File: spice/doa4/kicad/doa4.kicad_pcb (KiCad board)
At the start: 2 copper layers, 28 parts, among them Q1 BC557, Q10 BC547, Q11 BD139, Q12 BD140, Q2 BC557, Q3 BC547, Q4 BC547, Q5 BC557, Q6 BC547, Q7 BC547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

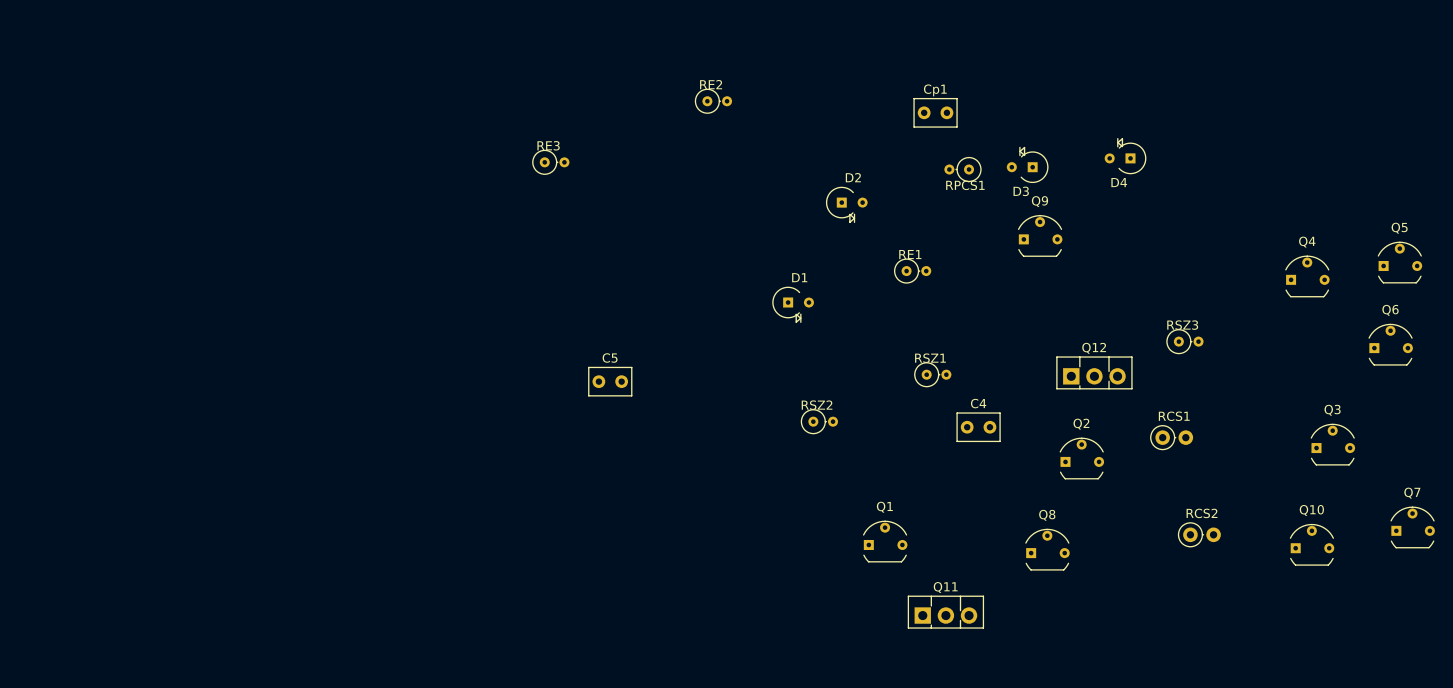
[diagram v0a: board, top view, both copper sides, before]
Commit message: init location input
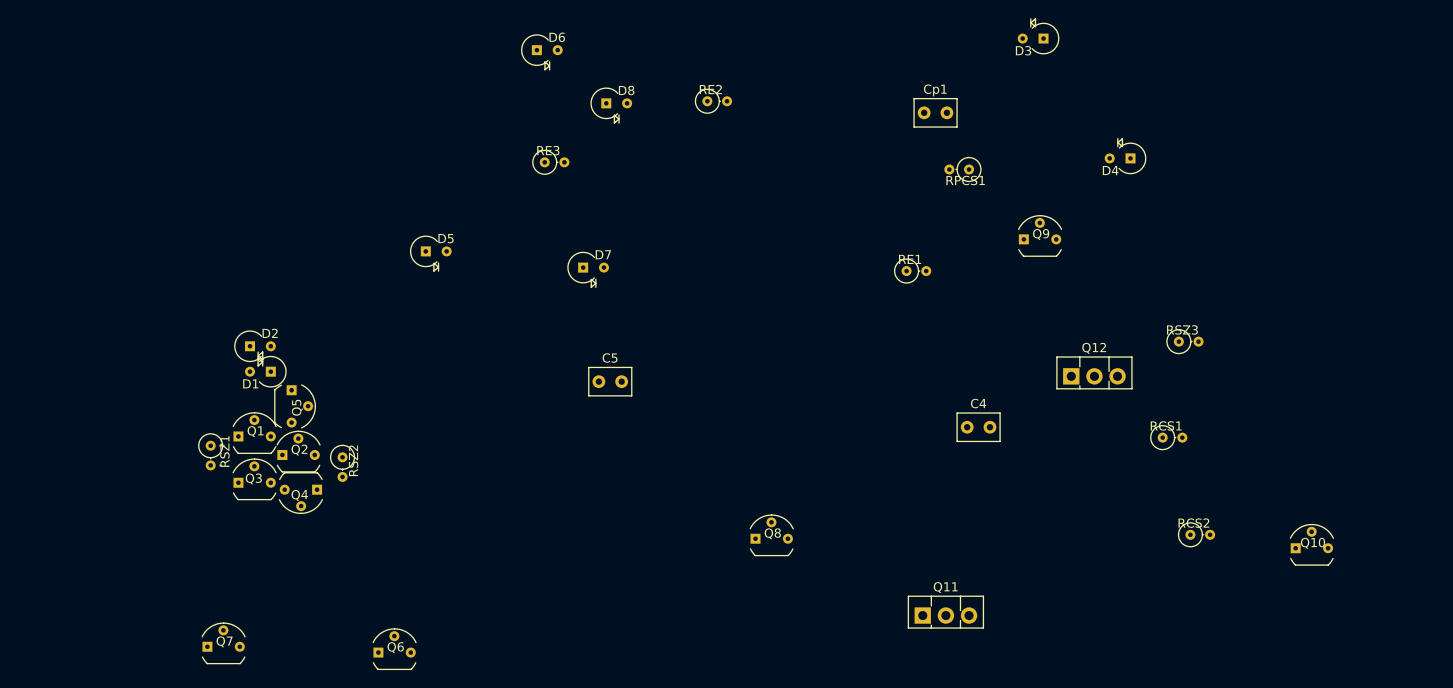
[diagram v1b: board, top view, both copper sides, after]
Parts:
- added D5: D1N4148, Doa4FPLibrary:D_DO-41_SOD81_P2.54mm_Vertical_AnodeUp_Doa4, F.Cu at (82.8, 71.9)
- added D6: D1N4148, Doa4FPLibrary:D_DO-41_SOD81_P2.54mm_Vertical_AnodeUp_Doa4, F.Cu at (95.0, 49.8)
- added D7: D1N4148, Doa4FPLibrary:D_DO-41_SOD81_P2.54mm_Vertical_AnodeUp_Doa4, F.Cu at (100.1, 73.7)
- added D8: D1N4148, Doa4FPLibrary:D_DO-41_SOD81_P2.54mm_Vertical_AnodeUp_Doa4, F.Cu at (102.6, 55.6)
- D3: value D14148 -> D1N4148
- D4: value D1418 -> D1N4148
- RCS1, RCS2: footprint Resistors_THT:R_Axial_DIN0207_L6.3mm_D2.5mm_P2.54mm_Vertical -> Doa4FPLibrary:R_Axial_DIN0207_L6.3mm_D2.5mm_P2.54mm_Vertical_Doa4
- moved Q7 131.1 mm to (58.1, 115.3)
- moved Q5 119.8 mm to (68.1, 86.4), turned to 270 degrees
- moved Q3 118.4 mm to (61.5, 97.3)
- moved Q6 114.3 mm to (76.8, 115.9)
- moved Q4 107.9 mm to (71.6, 98.0), turned to 180 degrees
- moved Q2 86.0 mm to (66.3, 94.2)
- moved RSZ1 79.0 mm to (59.2, 93.2), turned to 270 degrees
- moved Q1 70.2 mm to (61.5, 92.2)
- moved D2 66.9 mm to (63.5, 82.3)
- moved D1 57.3 mm to (65.8, 85.1), turned to 180 degrees
- moved RSZ2 51.8 mm to (73.7, 94.5), turned to 270 degrees
- moved Q8 30.3 mm to (118.2, 103.4)
- moved D3 14.2 mm to (150.6, 48.5)
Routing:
- net (no net): track 0.00 -> 0.58 mm

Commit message: conn j990 added
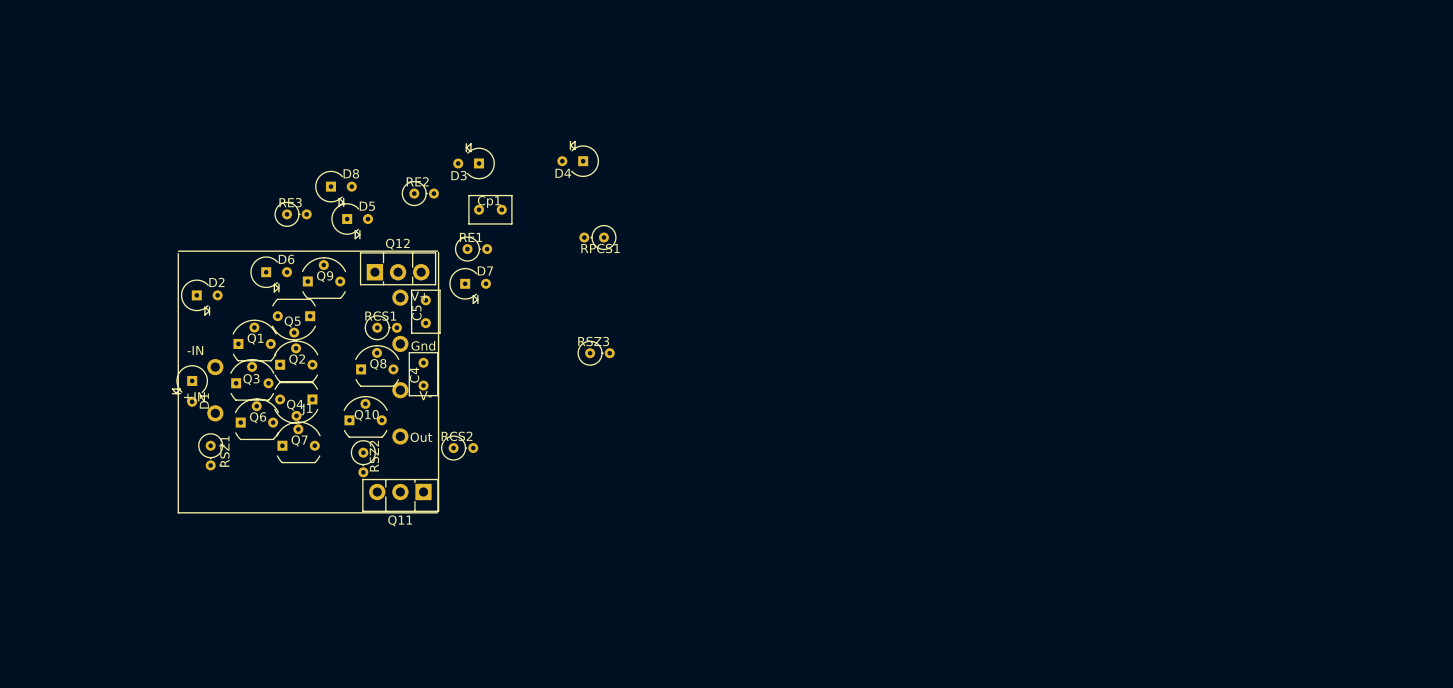
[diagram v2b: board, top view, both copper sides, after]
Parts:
- added J1: CONN_01X06, Doa4FPLibrary:j990, F.Cu at (69.8, 87.1)
- C4: footprint Capacitors_THT:C_Rect_L4.6mm_W3.0mm_P2.50mm_MKS02_FKP02 -> Doa4FPLibrary:C_Rect_L4.6mm_W3.0mm_P2.50mm_MKS02_FKP02_Doa4
- moved Q10 104.8 mm to (73.7, 90.4)
- moved RCS1 87.1 mm to (77.5, 80.3)
- moved RCS2 81.5 mm to (85.9, 93.5)
- moved Q9 78.7 mm to (69.1, 75.2)
- moved Q12 77.3 mm to (77.2, 74.2)
- moved RSZ3 64.7 mm to (100.8, 83.1)
- moved D3 63.5 mm to (88.6, 62.2)
- moved D4 60.1 mm to (100.1, 62.0)
- moved C4 59.9 mm to (82.5, 86.6), turned to 90 degrees
- moved Q11 56.5 mm to (82.5, 98.3), turned to 180 degrees
- moved Cp1 50.0 mm to (88.6, 67.3)
- moved RE1 48.3 mm to (87.4, 71.6)
- moved Q8 47.1 mm to (74.9, 84.8)
- moved RPCS1 40.8 mm to (102.4, 70.4)
- moved D6 38.4 mm to (65.3, 74.2)
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
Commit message: location init
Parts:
- added RCP1: 380, Doa4FPLibrary:R_Axial_DIN0207_L6.3mm_D2.5mm_P2.54mm_Vertical_Doa4, F.Cu at (64.0, 72.9)
- moved D4 43.3 mm to (58.4, 73.7), turned to 0 degrees
- moved D3 32.6 mm to (58.9, 75.7), turned to 270 degrees
- moved Q6 32.1 mm to (93.7, 93.2), turned to 270 degrees
- moved RSZ3 31.3 mm to (73.7, 98.6), turned to 180 degrees
- moved RE3 28.8 mm to (77.0, 95.0)
- moved RPCS1 28.6 mm to (73.9, 73.4)
- moved Cp1 28.0 mm to (62.0, 75.9)
- moved Q12 24.9 mm to (77.5, 99.1)
- moved Q11 24.9 mm to (82.5, 73.4)
- moved RCS1 21.3 mm to (56.6, 75.9), turned to 270 degrees
- moved D6 20.9 mm to (71.1, 94.2)
- moved RE1 17.0 mm to (70.9, 75.7)
- moved RCS2 16.7 mm to (88.4, 77.0), turned to 270 degrees
- moved Q9 15.3 mm to (74.7, 89.4)
- moved Q5 15.2 mm to (55.9, 81.3), turned to 0 degrees
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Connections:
- Cp1 pad 1: /ODiff -> Net-(Cp1-Pad1)
- Q10 pad 1: Net-(Cp1-Pad2) -> Net-(Q10-Pad1)
- Q9 pad 2: Net-(Cp1-Pad2) -> Net-(Q10-Pad1)
- RSZ3 pad 1: Net-(Cp1-Pad2) -> Net-(Q10-Pad1)
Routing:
- net /In-: track 0.00 -> 6.48 mm
- net /In+: track 0.00 -> 5.85 mm
- net (no net): track 0.58 -> 0.00 mm

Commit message: location init 2
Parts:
- moved Q6 31.1 mm to (63.1, 87.9)
- moved D4 29.2 mm to (73.4, 98.7), turned to 180 degrees
- moved Q8 25.1 mm to (65.4, 76.6)
- moved RCS1 23.8 mm to (72.9, 93.3)
- moved Q4 23.2 mm to (55.8, 76.6), turned to 0 degrees
- moved RCS2 23.2 mm to (65.5, 73.0), turned to 180 degrees
- moved Q5 21.4 mm to (69.5, 97.8), turned to 180 degrees
- moved D3 20.2 mm to (67.2, 94.1), turned to 0 degrees
- moved RSZ3 18.1 mm to (66.2, 82.0), turned to 0 degrees
- moved RSZ2 17.8 mm to (62.4, 76.6)
- moved RCP1 16.3 mm to (72.4, 86.9), turned to 180 degrees
- moved RE1 14.8 mm to (74.3, 90.0)
- moved Q2 13.1 mm to (60.8, 80.4), turned to 180 degrees
- moved Cp1 12.0 mm to (71.5, 83.3)
- moved Q10 7.59 mm to (66.3, 88.5)
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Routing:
- net /In-: track 6.48 -> 0.00 mm
- net /In+: track 5.85 -> 0.00 mm

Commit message: location init 3 power
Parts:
- moved D3 2.57 mm to (69.7, 94.5), turned to 180 degrees
- moved Q7 1.26 mm to (63.9, 84.1)
- moved RSZ3 1.15 mm to (67.3, 82.2)
- moved RSZ2 1.02 mm to (62.9, 75.7)
- moved Q4 0.92 mm to (56.5, 76.1)
- moved Q2 0.91 mm to (61.6, 79.9)
- moved Q5 0.74 mm to (69.1, 97.2)
- moved Q11 0.72 mm to (82.0, 73.9)
- moved Q9 0.63 mm to (69.1, 92.8)
- moved RCP1 0.63 mm to (72.9, 86.5)
- moved Q6 0.61 mm to (63.7, 87.9)
- moved Q12 0.54 mm to (77.1, 98.7)
- moved RCS2 0.54 mm to (65.2, 73.4)
- moved RE3 0.54 mm to (80.8, 94.9)
- moved Q3 0.28 mm to (61.5, 97.4)
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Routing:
- net /V-: track 0.00 -> 30.6 mm
- net /V+: track 0.00 -> 19.9 mm
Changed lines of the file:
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@@
   (general
     (links 60)
-    (no_connects 60)
+    (no_connects 54)
     (area 52.478438 69.161 84.8315 103.405)
     (thickness 1.6)
     (drawings 0)
-    (tracks 0)
+    (tracks 17)
     (zones 0)
     (modules 34)
@@
     (44 Edge.Cuts user hide)
     (45 Margin user)
-    (46 B.CrtYd user)
+    (46 B.CrtYd user hide)
     (47 F.CrtYd user hide)
     (48 B.Fab user hide)
@@
   )
   (module Doa4FPLibrary:TO-126_Vertical_Doa4 (layer F.Cu)
-    (at 82.55 73.406 180)
+    (at 82.042 73.914 180)
     (descr "TO-126, Vertical, RM 2.54mm")
     (tags "TO-126 Vertical RM 2.54mm")
@@
   )
   (module Doa4FPLibrary:TO-126_Vertical_Doa4 (layer F.Cu)
-    (at 77.47 99.06)
+    (at 77.089 98.679)
     (descr "TO-126, Vertical, RM 2.54mm")
     (tags "TO-126 Vertical RM 2.54mm")
@@
   )
   (module Doa4FPLibrary:TO-92_Molded_Wide_BCXXX (layer F.Cu)
-    (at 66.294 88.519 90)
+    (at 66.548 88.646 90)
     (descr "TO-92 leads molded, wide, drill 0.8mm (see NXP sot054_po.pdf)")
     (tags "to-92 sc-43 sc-43a sot54 PA33 transistor")
@@
   )
   (module Doa4FPLibrary:TO-92_Molded_Wide_BCXXX (layer F.Cu)
-    (at 68.58 93.218 90)
+    (at 69.088 92.837 90)
     (descr "TO-92 leads molded, wide, drill 0.8mm (see NXP sot054_po.pdf)")
     (tags "to-92 sc-43 sc-43a sot54 PA33 transistor")
@@
   )
   (module Doa4FPLibrary:TO-92_Molded_Wide_BCXXX (layer F.Cu)
-    (at 62.992 84.963 90)
+    (at 63.881 84.074 90)
     (descr "TO-92 leads molded, wide, drill 0.8mm (see NXP sot054_po.pdf)")
     (tags "to-92 sc-43 sc-43a sot54 PA33 transistor")
@@
   )
   (module Doa4FPLibrary:TO-92_Molded_Wide_BCXXX (layer F.Cu)
-    (at 63.119 87.884 270)
+    (at 63.7286 87.9094 270)
     (descr "TO-92 leads molded, wide, drill 0.8mm (see NXP sot054_po.pdf)")
     (tags "to-92 sc-43 sc-43a sot54 PA33 transistor")
@@
   )
   (module Doa4FPLibrary:TO-92_Molded_Wide_BCXXX (layer F.Cu)
-    (at 69.469 97.79 180)
+    (at 69.088 97.155 180)
     (descr "TO-92 leads molded, wide, drill 0.8mm (see NXP sot054_po.pdf)")
     (tags "to-92 sc-43 sc-43a sot54 PA33 transistor")
@@
   )
   (module Doa4FPLibrary:TO-92_Molded_Wide_BCXXX (layer F.Cu)
-    (at 55.753 76.581)
+    (at 56.515 76.073)
     (descr "TO-92 leads molded, wide, drill 0.8mm (see NXP sot054_po.pdf)")
     (tags "to-92 sc-43 sc-43a sot54 PA33 transistor")
@@
   )
   (module Doa4FPLibrary:TO-92_Molded_Wide_BCXXX (layer F.Cu)
-    (at 61.214 97.282 180)
+    (at 61.468 97.409 180)
     (descr "TO-92 leads molded, wide, drill 0.8mm (see NXP sot054_po.pdf)")
     (tags "to-92 sc-43 sc-43a sot54 PA33 transistor")
@@
   )
   (module Doa4FPLibrary:TO-92_Molded_Wide_BCXXX (layer F.Cu)
-    (at 60.833 80.391 180)
+    (at 61.5696 79.8576 180)
     (descr "TO-92 leads molded, wide, drill 0.8mm (see NXP sot054_po.pdf)")
     (tags "to-92 sc-43 sc-43a sot54 PA33 transistor")
@@
   )
   (module Doa4FPLibrary:TO-92_Molded_Wide_BCXXX (layer F.Cu)
-    (at 56.134 93.472)
+    (at 56.388 93.472)
     (descr "TO-92 leads molded, wide, drill 0.8mm (see NXP sot054_po.pdf)")
     (tags "to-92 sc-43 sc-43a sot54 PA33 transistor")
@@
   )
   (module Doa4FPLibrary:R_Axial_DIN0207_L6.3mm_D2.5mm_P2.54mm_Vertical_Doa4 (layer F.Cu)
-    (at 62.357 76.581 270)
+    (at 62.865 75.692 270)
     (descr "Resistor, Axial_DIN0207 series, Axial, Vertical, pin pitch=2.54mm, 0.25W = 1/4W, length*diameter=6.3*2.5mm^2, http://cdn-reichelt.de/documents/datenblatt/B400/1_4W%23YAG.pdf")
     (tags "Resistor Axial_DIN0207 series Axial Vertical pin pitch 2.54mm 0.25W = 1/4W length 6.3mm diameter 2.5mm")
@@
   )
   (module Doa4FPLibrary:R_Axial_DIN0207_L6.3mm_D2.5mm_P2.54mm_Vertical_Doa4 (layer F.Cu)
-    (at 65.532 73.025 180)
+    (at 65.151 73.406 180)
     (descr "Resistor, Axial_DIN0207 series, Axial, Vertical, pin pitch=2.54mm, 0.25W = 1/4W, length*diameter=6.3*2.5mm^2, http://cdn-reichelt.de/documents/datenblatt/B400/1_4W%23YAG.pdf")
     (tags "Resistor Axial_DIN0207 series Axial Vertical pin pitch 2.54mm 0.25W = 1/4W length 6.3mm diameter 2.5mm")
@@
   )
   (module Doa4FPLibrary:R_Axial_DIN0207_L6.3mm_D2.5mm_P2.54mm_Vertical_Doa4 (layer F.Cu)
-    (at 66.167 82.042)
+    (at 67.31 82.169)
     (descr "Resistor, Axial_DIN0207 series, Axial, Vertical, pin pitch=2.54mm, 0.25W = 1/4W, length*diameter=6.3*2.5mm^2, http://cdn-reichelt.de/documents/datenblatt/B400/1_4W%23YAG.pdf")
     (tags "Resistor Axial_DIN0207 series Axial Vertical pin pitch 2.54mm 0.25W = 1/4W length 6.3mm diameter 2.5mm")
@@
   )
   (module Doa4FPLibrary:R_Axial_DIN0207_L6.3mm_D2.5mm_P2.54mm_Vertical_Doa4 (layer F.Cu)
-    (at 81.153 95.25)
+    (at 80.772 94.869)
     (descr "Resistor, Axial_DIN0207 series, Axial, Vertical, pin pitch=2.54mm, 0.25W = 1/4W, length*diameter=6.3*2.5mm^2, http://cdn-reichelt.de/documents/datenblatt/B400/1_4W%23YAG.pdf")
     (tags "Resistor Axial_DIN0207 series Axial Vertical pin pitch 2.54mm 0.25W = 1/4W length 6.3mm diameter 2.5mm")
@@
   )
   (module Doa4FPLibrary:D_DO-41_SOD81_P2.54mm_Vertical_AnodeUp_Doa4 (layer F.Cu)
-    (at 67.183 94.107)
+    (at 69.723 94.488 180)
     (descr "D, DO-41_SOD81 series, Axial, Vertical, pin pitch=2.54mm, , length*diameter=5.2*2.7mm^2, , http://www.diodes.com/_files/packages/DO-41%20(Plastic).pdf")
     (tags "D DO-41_SOD81 series Axial Vertical pin pitch 2.54mm  length 5.2mm diameter 2.7mm")
-    (fp_text reference D3 (at 2.2098 -1.3716) (layer F.SilkS)
-      (effects (font (size 1 1) (thickness 0.15)))
-    )
-    (fp_text value D1N4148 (at 0.9398 1.0668) (layer F.Fab)
+    (fp_text reference D3 (at 2.2098 -1.3716 180) (layer F.SilkS)
+      (effects (font (size 1 1) (thickness 0.15)))
+    )
+    (fp_text value D1N4148 (at 0.9398 1.0668 180) (layer F.Fab)
       (effects (font (size 1 1) (thickness 0.15)))
     )
@@
     (fp_line (start 0 0) (end 2.54 0) (layer F.Fab) (width 0.1))
     (fp_line (start 1.397 1.28) (end 1.397 2.169) (layer F.SilkS) (width 0.12))
-    (fp_text user K (at 3.2512 0) (layer F.Fab)
-      (effects (font (size 1 1) (thickness 0.15)))
-    )
-    (pad 1 thru_hole rect (at 0 0) (size 1.1 1.1) (drill 0.5) (layers *.Cu *.Mask)
+    (fp_text user K (at 3.2512 0 180) (layer F.Fab)
+      (effects (font (size 1 1) (thickness 0.15)))
+    )
+    (pad 1 thru_hole rect (at 0 0 180) (size 1.1 1.1) (drill 0.5) (layers *.Cu *.Mask)
       (net 21 "Net-(D3-Pad1)"))
-    (pad 2 thru_hole oval (at 2.286 0) (size 1.1 1.1) (drill 0.5) (layers *.Cu *.Mask)
+    (pad 2 thru_hole oval (at 2.286 0 180) (size 1.1 1.1) (drill 0.5) (layers *.Cu *.Mask)
       (net 9 /VrefCS))
     (model Diodes_THT.3dshapes/D_DO-41_SOD81_P2.54mm_Vertical_AnodeUp.wrl
@@
   )
   (module Doa4FPLibrary:C_Rect_L4.6mm_W3.0mm_P2.50mm_MKS02_FKP02_Doa4 (layer F.Cu)
-    (at 82.804 83.82 270)
+    (at 82.55 83.86 270)
     (descr "C, Rect series, Radial, pin pitch=2.50mm, , length*width=4.6*3.0mm^2, Capacitor, http://www.wima.de/DE/WIMA_MKS_02.pdf")
     (tags "C Rect series Radial pin pitch 2.50mm  length 4.6mm width 3.0mm Capacitor")
@@
   )
   (module Doa4FPLibrary:C_Rect_L4.6mm_W3.0mm_P2.50mm_MKS02_FKP02_Doa4 (layer F.Cu)
-    (at 82.804 78.486 270)
+    (at 82.55 78.486 270)
     (descr "C, Rect series, Radial, pin pitch=2.50mm, , length*width=4.6*3.0mm^2, Capacitor, http://www.wima.de/DE/WIMA_MKS_02.pdf")
     (tags "C Rect series Radial pin pitch 2.50mm  length 4.6mm width 3.0mm Capacitor")
@@
   )
   (module Doa4FPLibrary:R_Axial_DIN0207_L6.3mm_D2.5mm_P2.54mm_Vertical_Doa4 (layer F.Cu)
-    (at 72.39 86.868 180)
+    (at 72.898 86.487 180)
     (descr "Resistor, Axial_DIN0207 series, Axial, Vertical, pin pitch=2.54mm, 0.25W = 1/4W, length*diameter=6.3*2.5mm^2, http://cdn-reichelt.de/documents/datenblatt/B400/1_4W%23YAG.pdf")
     (tags "Resistor Axial_DIN0207 series Axial Vertical pin pitch 2.54mm 0.25W = 1/4W length 6.3mm diameter 2.5mm")
@@
     )
   )
+  (segment (start 73.318001 96.379001) (end 73.773001 95.924001) (width 0.25) (layer B.Cu) (net 1))
+  (segment (start 72.124997 96.379001) (end 73.318001 96.379001) (width 0.25) (layer B.Cu) (net 1))
+  (segment (start 73.773001 94.220001) (end 73.447999 93.894999) (width 0.25) (layer B.Cu) (net 1))
+  (segment (start 73.447999 93.894999) (end 72.898 93.345) (width 0.25) (layer B.Cu) (net 1))
+  (segment (start 73.773001 95.924001) (end 73.773001 94.220001) (width 0.25) (layer B.Cu) (net 1))
+  (segment (start 73.406 98.679) (end 73.406 96.52) (width 0.25) (layer B.Cu) (net 1))
+  (segment (start 79.121001 76.073001) (end 70.510003 76.073001) (width 0.25) (layer B.Cu) (net 1))
+  (segment (start 70.510003 76.073001) (end 67.462002 73.025) (width 0.25) (layer B.Cu) (net 1))
+  (segment (start 83.775001 74.422) (end 83.775001 72.245999) (width 0.25) (layer B.Cu) (net 11))
+  (segment (start 83.775001 74.566001) (end 83.775001 74.422) (width 0.25) (layer B.Cu) (net 11))
+  (segment (start 83.775001 74.422) (end 83.775001 85.348999) (width 0.25) (layer B.Cu) (net 11))
+  (segment (start 83.710001 72.180999) (end 72.980001 72.180999) (width 0.25) (layer B.Cu) (net 11))
+  (segment (start 83.775001 72.245999) (end 83.710001 72.180999) (width 0.25) (layer B.Cu) (net 11))
+  (segment (start 72.980001 72.180999) (end 72.304999 72.856001) (width 0.25) (layer B.Cu) (net 11))
+  (segment (start 72.304999 72.856001) (end 71.755 73.406) (width 0.25) (layer B.Cu) (net 11))
+  (segment (start 80.01 87.122) (end 77.089 90.043) (width 0.25) (layer B.Cu) (net 11))
+  (segment (start 77.089 90.043) (end 76.454 90.043) (width 0.25) (layer B.Cu) (net 11))
 )

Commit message: location init 4 q9q10
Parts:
- moved Q9 9.93 mm to (73.4, 83.9), turned to 270 degrees
- moved RCP1 7.53 mm to (66.4, 82.6), turned to 0 degrees
- moved Cp1 7.02 mm to (65.7, 87.3), turned to 90 degrees
- moved RSZ3 3.21 mm to (70.5, 82.8)
- moved Q10 3.11 mm to (69.6, 89.0)
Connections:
- Cp1 pad 1: Net-(Cp1-Pad1) -> /ODiff
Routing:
- net /V-: track 30.6 -> 90.6 mm
- net Net-(Q4-Pad3): track 0.00 -> 31.6 mm
- net /VrefCS: track 0.00 -> 31.1 mm
- net /Emiter: track 0.00 -> 28.7 mm
- net /V+: track 19.9 -> 46.9 mm
- net Net-(D6-Pad2): track 0.00 -> 26.4 mm
- net /Out: track 0.00 -> 16.0 mm
- net /ODiff: track 0.00 -> 15.3 mm
- net Net-(Q10-Pad1): track 0.00 -> 14.0 mm
- net /In-: track 0.00 -> 11.6 mm
- net Net-(Q2-Pad1): track 0.00 -> 10.7 mm
- net Net-(D5-Pad2): track 0.00 -> 10.6 mm
- net Net-(Q1-Pad1): track 0.00 -> 9.02 mm
- net Net-(Q5-Pad3): track 0.00 -> 8.55 mm
- net /In+: track 0.00 -> 7.64 mm
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
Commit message: location  q8q5
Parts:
- moved RPCS1 40.0 mm to (39.4, 93.7), turned to 270 degrees
- moved D4 27.8 mm to (46.4, 92.3), turned to 270 degrees
- moved Q8 25.7 mm to (45.4, 92.7), turned to 180 degrees
- moved RCS1 24.3 mm to (48.6, 94.7)
- moved Q5 23.7 mm to (45.3, 97.0)
- moved D3 23.4 mm to (46.4, 96.6), turned to 270 degrees
- moved Q9 11.6 mm to (70.4, 95.1)
- moved Q10 11.6 mm to (66.6, 100.1)
- moved RSZ3 11.4 mm to (67.9, 93.9)
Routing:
- net /Emiter: track 28.7 -> 3.80 mm
- net Net-(D6-Pad2): track 26.4 -> 3.03 mm
- net /VrefCS: track 31.1 -> 11.8 mm
- net Net-(Q10-Pad1): track 14.0 -> 0.29 mm
- net /V-: track 90.6 -> 101.7 mm
- net Net-(Q4-Pad3): track 31.6 -> 22.2 mm
- net Net-(Q10-Pad3): track 5.95 -> 0.00 mm
- net /V+: track 46.9 -> 41.0 mm
- net /ODiff: track 15.3 -> 9.53 mm
- net Net-(Q11-Pad1): track 0.00 -> 5.50 mm
- net Net-(Q8-Pad3): track 4.49 -> 0.00 mm
- net Net-(Q5-Pad3): track 8.55 -> 4.58 mm
- net Net-(D3-Pad1): track 4.77 -> 2.08 mm
